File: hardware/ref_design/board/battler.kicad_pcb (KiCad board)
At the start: 2 copper layers, 73.4 x 151.5 mm, 173 parts, among them J1 TYPE-C-31-M-12, J2 53261-0271, J3 FH12-50S-0.5SH(55), J4 SM02B-SRSS-TB, J5 SWD, J7 DEBUG PADS, Q1 2N7002, Q3 2N7002, Q5 AO3400A, Q6 AO3400A, Q7 2N7002, SW1 P1 UP, SW10 P2 DOWN, SW11 P2 LEFT, SW12 P2 RIGHT, SW13 P2 A, SW14 P2 B, SW15 P2 X, SW16 P2 Y, SW18 BOOTSEL, SW19 RESET, SW2 P1 DOWN, SW20 P1 SELECT, SW21 P1 START / PWR, SW22 P2 SELECT, SW23 P2 START / PWR, SW3 P1 LEFT, SW4 P1 RIGHT, SW5 P1 A, SW6 P1 B, SW7 P1 X, SW8 P1 Y, SW9 P2 UP, U1 SRV05-4, U10 MCP6001, U2 BQ24073RGTR, U3 RT9013-33GB, U4 RP2354B, U6 MCP6002, U7 FM8002A, U8 SN74HC165PWR, U9 SN74HC165PWR, X1 12MHz

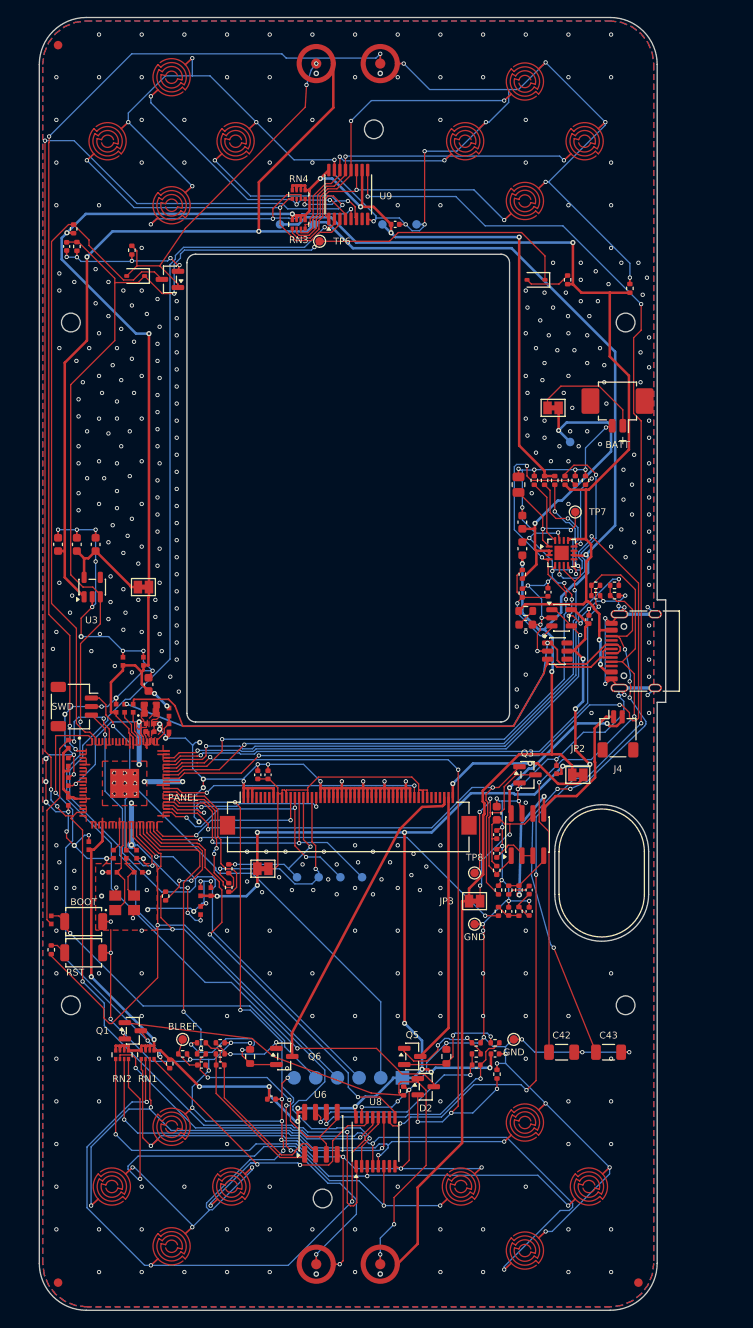
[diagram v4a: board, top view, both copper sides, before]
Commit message: ref_design ESP32-S3: first placement (module, microSD slot with trimmed front tabs, series resistors, third register; case grow_l 1.5 for the shell tabs' copper edge), BOOT/RESET buttons dropped (J7 pads stay), place_new.py, antenna keepout, module GND vias; not routed
Co-Authored-By: Claude Sonnet 5.5 <noreply@anthropic.com>
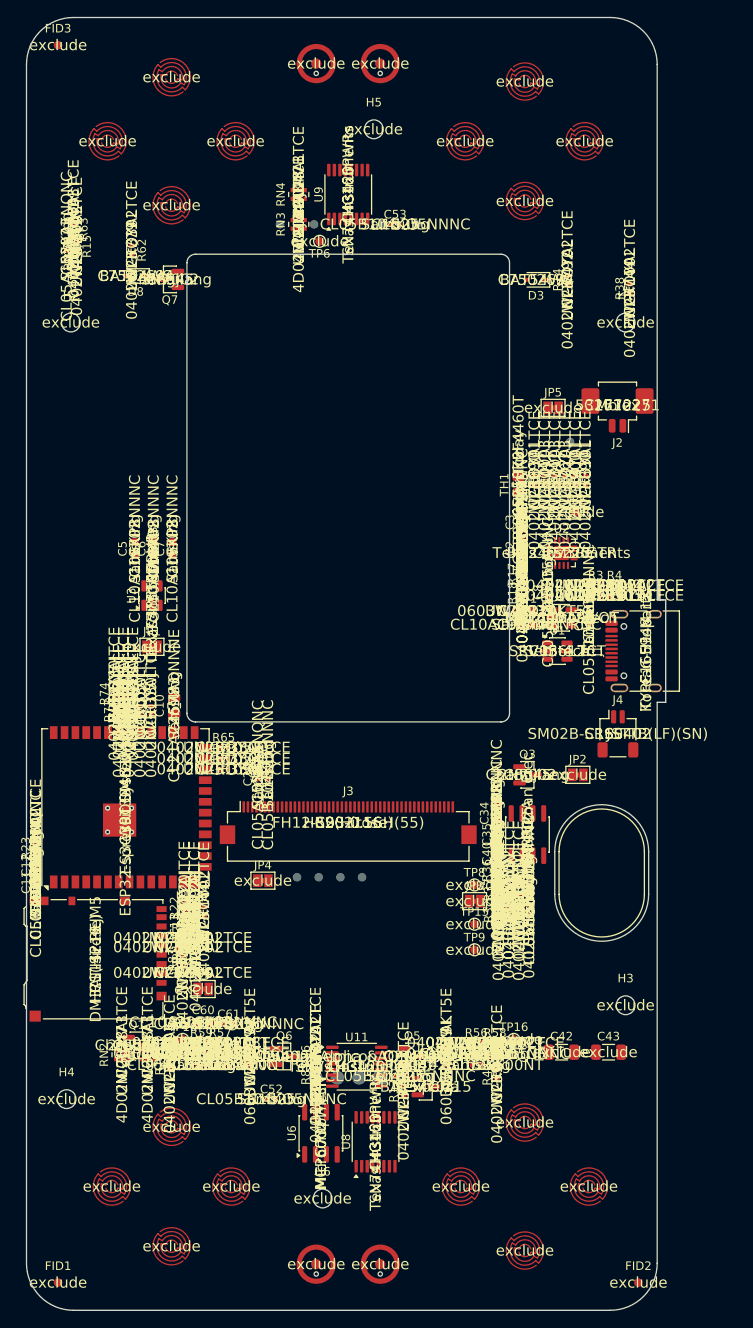
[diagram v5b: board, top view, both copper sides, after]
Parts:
- removed C15, C16, C17, C18, C19, C20, C21, C22: 100n, battler:C_0402_1005Metric_RPi
- removed C23: 10u, Capacitor_SMD:C_0603_1608Metric
- removed C24, C25: 4.7u, battler:C_0402_1005Metric_RPi_Wide
- removed C26: 4.7u, battler:C_0402_1005Metric_RPi
- removed C27, C28: 15p, battler:C_0402_1005Metric_RPi
- removed J5: SWD, battler:JST_SH_SM03B-SRSS-TB_1x03-1MP_P1.00mm_Horizontal
- removed L2: 3.3u, battler:AOTA-B201610S3R3-101-T
- removed R19: 33, battler:R_0402_1005Metric_RPi
- removed R20, R25: 1k, battler:R_0402_1005Metric_RPi
- removed R26: 1k, Resistor_SMD:R_0402_1005Metric
- removed R28, R29: 33, Resistor_SMD:R_0402_1005Metric
- removed SW18: BOOTSEL, battler:SW_SPST_TS-1088-xR020
- removed SW19: RESET, battler:SW_SPST_TS-1088-xR020
- removed X1: 12MHz, battler:ABM8-272-T3
- added C60: 10u, Capacitor_SMD:C_0603_1608Metric, F.Cu at (83.0, 142.0)
- added C61: 100n, Capacitor_SMD:C_0402_1005Metric, F.Cu at (86.0, 142.2)
- added C62: 100n, Capacitor_SMD:C_0402_1005Metric, F.Cu at (106.1, 148.3)
- added J8: DM3AT-SF-PEJM5, battler:microSD_HC_Hirose_DM3AT-SF-PEJM5, F.Cu at (70.4, 134.6)
- added JP6: Bridged, Jumper:SolderJumper-2_P1.3mm_Bridged_Pad1.0x1.5mm, F.Cu at (83.0, 138.1)
- added R70: 33, Resistor_SMD:R_0402_1005Metric, F.Cu at (76.9, 105.5)
- added R71: 33, Resistor_SMD:R_0402_1005Metric, F.Cu at (75.6, 105.5)
- added R72: 33, Resistor_SMD:R_0402_1005Metric, F.Cu at (74.3, 105.5)
- added R73: 33, Resistor_SMD:R_0402_1005Metric, F.Cu at (73.1, 105.5)
- added R74: 33, Resistor_SMD:R_0402_1005Metric, F.Cu at (72.6, 103.5)
- added R75: 33, Resistor_SMD:R_0402_1005Metric, F.Cu at (73.7, 103.5)
- added R76: 33, Resistor_SMD:R_0402_1005Metric, F.Cu at (74.8, 103.5)
- added R77: 33, Resistor_SMD:R_0402_1005Metric, F.Cu at (85.4, 112.4)
- added R78: 33, Resistor_SMD:R_0402_1005Metric, F.Cu at (85.4, 111.1)
- added R79: 10k, Resistor_SMD:R_0402_1005Metric, F.Cu at (83.1, 129.0)
- added R80: 10k, Resistor_SMD:R_0402_1005Metric, F.Cu at (80.6, 132.1)
- added R81: 10k, Resistor_SMD:R_0402_1005Metric, F.Cu at (82.1, 132.6)
- added R82: 10k, Resistor_SMD:R_0402_1005Metric, F.Cu at (80.6, 133.2)
- added R83: 10k, Resistor_SMD:R_0402_1005Metric, F.Cu at (80.6, 134.7)
- added R84: 10k, Resistor_SMD:R_0402_1005Metric, F.Cu at (80.6, 136.2)
- added R86: 47k, Resistor_SMD:R_0402_1005Metric, F.Cu at (96.2, 146.0)
- added R87: 47k, Resistor_SMD:R_0402_1005Metric, F.Cu at (96.2, 148.0)
- added U11: SN74HC165PWR, Package_SO:TSSOP-16_4.4x5mm_P0.65mm, F.Cu at (101.0, 147.2)
- C10: value 100n -> 22u; footprint battler:C_0402_1005Metric_RPi -> Capacitor_SMD:C_0805_2012Metric
- C11: footprint battler:C_0402_1005Metric_RPi -> Capacitor_SMD:C_0402_1005Metric
- C12: value 100n -> 1u; footprint battler:C_0402_1005Metric_RPi -> Capacitor_SMD:C_0402_1005Metric
- C13, C14: value 100n -> DNP; footprint battler:C_0402_1005Metric_RPi -> Capacitor_SMD:C_0402_1005Metric
- J7: footprint battler:Pogo_Pads_1x06_P2.54mm -> battler:Pogo_Pads_1x04_P2.54mm
- R21, R22: value 27 -> 22; footprint battler:R_0402_1005Metric_RPi -> Resistor_SMD:R_0402_1005Metric
- R23: footprint battler:R_0402_1005Metric_RPi -> Resistor_SMD:R_0402_1005Metric
- R32, R33: value 1k -> 1.5k
- TP11: value LCD_SCK -> LCD_WR
- TP12: value LCD_MOSI -> LCD_DC
- TP13: value LCD_CS -> LCD_D0
- TP14: value LCD_DC -> LCD_TE
- TP9: value +1V1 -> AUDIO_PWM; moved to F.Cu
- U3: value RT9013-33GB -> TLV75733PDBVR
- U4: value RP2354B -> ESP32-S3-WROOM-1U-N16R8; footprint battler:RP2350B_QFN80_RPi -> battler:ESP32-S3-WROOM-1U
- moved C10 45.4 mm to (79.6, 104.9)
- moved TP9 42.0 mm to (114.8, 133.5), turned to 0 degrees
- moved C13 31.3 mm to (80.8, 130.6)
- moved R21 24.8 mm to (82.0, 128.6), turned to 90 degrees
- moved C14 24.2 mm to (82.0, 130.6)
- moved R22 24.2 mm to (80.8, 128.6), turned to 90 degrees
- moved C11 22.5 mm to (63.4, 125.6)
- moved R65 18.7 mm to (85.4, 109.8), turned to 0 degrees
- moved R23 12.8 mm to (63.4, 121.6)
- moved H4 11.0 mm to (67.0, 151.0)
- moved C12 9.19 mm to (63.4, 123.6), turned to 90 degrees
- moved C5 9.01 mm to (75.0, 86.5)
- moved C6 9.01 mm to (77.2, 86.5)
- moved C7 9.01 mm to (79.4, 86.5)
- moved JP1 7.07 mm to (77.0, 98.0)
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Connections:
- net /Display/LCD_SCK renamed /Display/LCD_WR
- C12 pad 1: +3V3 -> EN
- C13 pad 1: +3V3 -> /MCU/USB_DP_MCU
- C14 pad 1: +3V3 -> /MCU/USB_DM_MCU
- J3 pad 13: LCD_CS -> GND
- J3 pad 17: /Display/LCD_MOSI -> GND
- J3 pad 18: LCD_MISO -> unconnected-(J3-Pin_18-Pad18)
- J3 pad 19: GND -> /Display/LCD_D0
- J3 pad 20: GND -> /Display/LCD_D1
- J3 pad 21: GND -> /Display/LCD_D2
- J3 pad 22: GND -> /Display/LCD_D3
- J3 pad 23: GND -> /Display/LCD_D4
- J3 pad 24: GND -> /Display/LCD_D5
- J3 pad 25: GND -> /Display/LCD_D6
- J3 pad 26: GND -> /Display/LCD_D7
- J3 pad 42: /Display/LCD_3V3 -> GND
- J7 pad 2: SWCLK -> EN
- J7 pad 3: SWDIO -> BOOT
- J7 pad 4: RUN -> GND
- R23 pad 2: QSPI_SS -> EN
- SW20 pad 1: P1_SELECT -> /Buttons/P1_SELECT
- SW22 pad 1: P2_SELECT -> /Buttons/P2_SELECT
- TP12 pad 1: /Display/LCD_MOSI -> LCD_DC
- TP13 pad 1: LCD_CS -> /Display/LCD_D0
- TP14 pad 1: LCD_DC -> LCD_TE
- TP9 pad 1: +1V1 -> AUDIO_PWM
- U4 pad 1: P2_SELECT -> GND
- U4 pad 10: +1V1 -> SD_CD
- U4 pad 11: unconnected-(U4-GPIO12-Pad11) -> SR_CLK_MCU
- U4 pad 12: unconnected-(U4-GPIO13-Pad12) -> AUDIO_PWM
- U4 pad 13: unconnected-(U4-GPIO14-Pad13) -> /MCU/USB_DM_MCU
- U4 pad 14: unconnected-(U4-GPIO15-Pad14) -> /MCU/USB_DP_MCU
- U4 pad 15: +3V3 -> SR_DATA
- U4 pad 16: unconnected-(U4-GPIO16-Pad16) -> CHG_OFF
- U4 pad 17: unconnected-(U4-GPIO17-Pad17) -> BL_PWM
- U4 pad 18: unconnected-(U4-GPIO18-Pad18) -> LCD_TE
- U4 pad 19: SR_PL -> SD_CMD
- U4 pad 2: unconnected-(U4-GPIO5-Pad2) -> +3V3
- U4 pad 20: unconnected-(U4-GPIO20-Pad20) -> SD_CLK
- U4 pad 21: unconnected-(U4-GPIO21-Pad21) -> SD_D0
- U4 pad 22: unconnected-(U4-GPIO22-Pad22) -> SD_D1
- U4 pad 23: unconnected-(U4-GPIO23-Pad23) -> PWR_HOLD
- U4 pad 24: +3V3 -> LCD_D7_MCU
- U4 pad 25: unconnected-(U4-GPIO24-Pad25) -> LCD_WR_MCU
- U4 pad 26: unconnected-(U4-GPIO25-Pad26) -> AMP_EN
- U4 pad 27: unconnected-(U4-GPIO26-Pad27) -> BOOT
- U4 pad 29: +3V3 -> unconnected-(U4-IO36-Pad29)
- U4 pad 3: unconnected-(U4-GPIO6-Pad3) -> EN
- U4 pad 30: /MCU/XIN -> unconnected-(U4-IO37-Pad30)
- U4 pad 31: /MCU/XOUT -> LCD_D0_MCU
- U4 pad 32: +1V1 -> LCD_D1_MCU
- U4 pad 33: SWCLK -> LCD_D2_MCU
- U4 pad 34: SWDIO -> LCD_D3_MCU
- U4 pad 35: RUN -> LCD_D4_MCU
- U4 pad 36: BL_PWM -> LCD_D6_MCU
- U4 pad 37: SR_CLK_MCU -> LCD_D5_MCU
- U4 pad 38: SR_DATA -> CC1_SENSE
- U4 pad 39: AUDIO_PWM -> VBAT_SENSE
- U4 pad 4: unconnected-(U4-GPIO7-Pad4) -> CC2_SENSE
- U4 pad 40: LCD_TE -> GND
- U4 pad 41: +3V3 -> GND
- U4 pad 5: +3V3 -> SR_PL
- U4 pad 6: unconnected-(U4-GPIO8-Pad6) -> LCD_DC
- U4 pad 7: unconnected-(U4-GPIO9-Pad7) -> LCD_RST
- U4 pad 8: unconnected-(U4-GPIO10-Pad8) -> SD_D2
- U4 pad 9: unconnected-(U4-GPIO11-Pad9) -> SD_D3
- U9 pad 10: +3V3 -> /Buttons/SR_CHAIN2
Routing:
- net GND: track 750.2 -> 0.00 mm, vias 498 -> 4
- net +3V3: track 406.7 -> 0.00 mm, vias 28 -> 0
- net VSYS: track 273.5 -> 0.00 mm, vias 5 -> 0
- net SR_PL: track 199.7 -> 0.00 mm, vias 6 -> 0
- net /Power/PWR_EN: track 195.4 -> 0.00 mm, vias 4 -> 0
- net /Buttons/SR_CLK: track 162.0 -> 0.00 mm, vias 3 -> 0
- net /Buttons/SR_CHAIN: track 158.7 -> 0.00 mm, vias 6 -> 0
- net P2_SELECT: track 118.5 -> 0.00 mm, vias 4 -> 0
- net VBUS: track 113.0 -> 0.00 mm, vias 3 -> 0
- net CHG_STAT_N: track 102.8 -> 0.00 mm, vias 5 -> 0
- net PWR_HOLD: track 91.1 -> 0.00 mm, vias 5 -> 0
- net CHG_OFF: track 88.8 -> 0.00 mm, vias 4 -> 0
- net CHG_PG_N: track 80.4 -> 0.00 mm, vias 4 -> 0
- net P2_START: track 78.7 -> 0.00 mm
- net SWCLK: track 78.6 -> 0.00 mm, vias 2 -> 0
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- removed copper zone on F.Cu, net +1V1
- removed copper zone on F.Cu, net +3V3
- removed copper zone on B.Cu, net GND
- removed copper zone on F.Cu, net GND
- removed copper zone on F.Cu, net VREG_LX
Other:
- board size 73.4 x 151.5 mm -> 74.9 x 151.5 mm
- board text removed: "+"
- board text removed: "1V1"
- board text removed: "2 LAYERS 1.6 MM ENIG"
- board text removed: "3V3"
- board text removed: "BATT"
- board text removed: "BLREF"
- board text removed: "BOOT"
- board text removed: "CS"
- board text removed: "DC"
- board text removed: "GND"
- board text removed: "MOSI"
- board text removed: "PANEL"
- board text removed: "REV 1"
- board text removed: "RST"
- board text removed: "SCK"
- board text removed: "SWD"
- board text removed: "SWD PADS"
- board text removed: "TWO-PLAYER HANDHELD REF-A"
- board text removed: "VBAT"
- board text removed: "VBUS"
- board text removed: "VSYS"

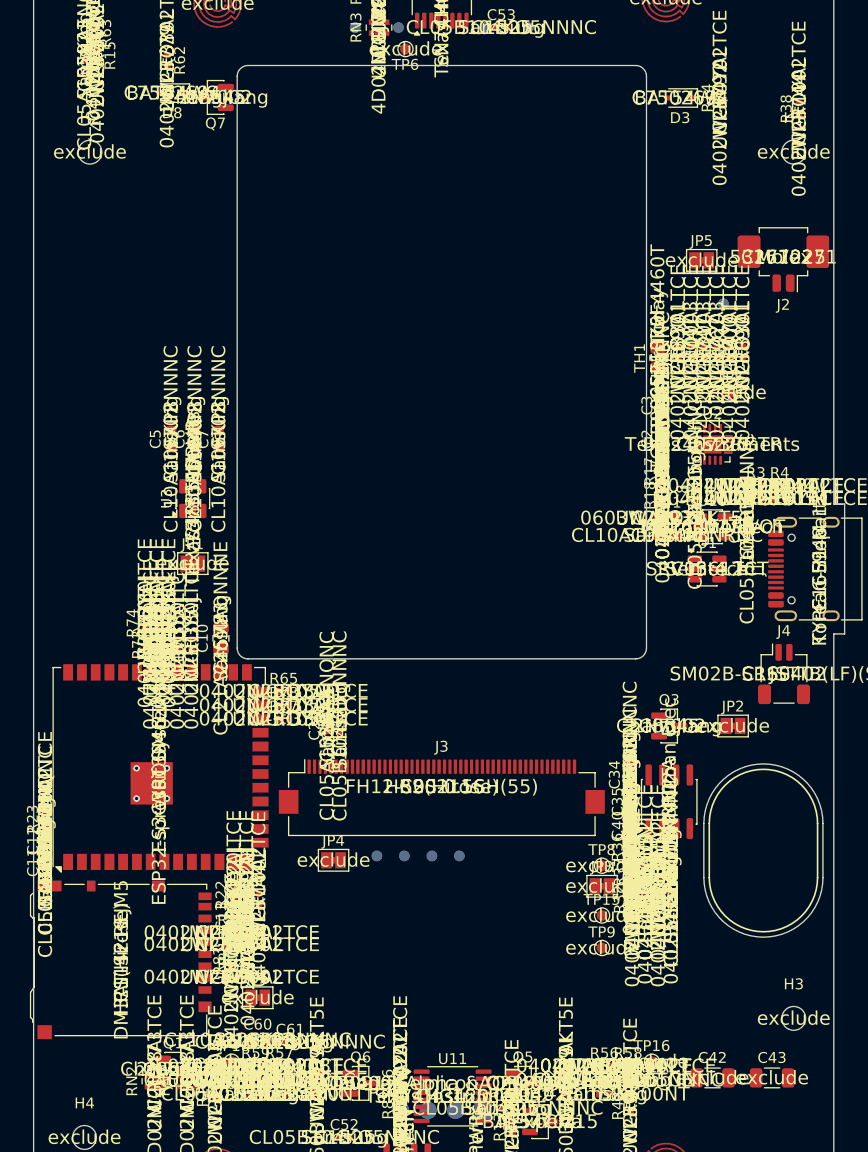
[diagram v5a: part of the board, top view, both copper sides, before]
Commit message: ref_design ESP32-S3 placement: module, microSD slot, nearest-legal-spot search for the new parts (tools/place_new.py), cell hole 38.2 x 55.2 (V&V C1), U2 on TI's RGT0016C land (P3), net classes for CELL_P, AMP_VDD, VBUS_C1 (P4), comb keep-out 2.9 flats (B3), check_fit module body; check_fit PASS, placement DRC clean
Co-Authored-By: Claude Sonnet 5.5 <noreply@anthropic.com>
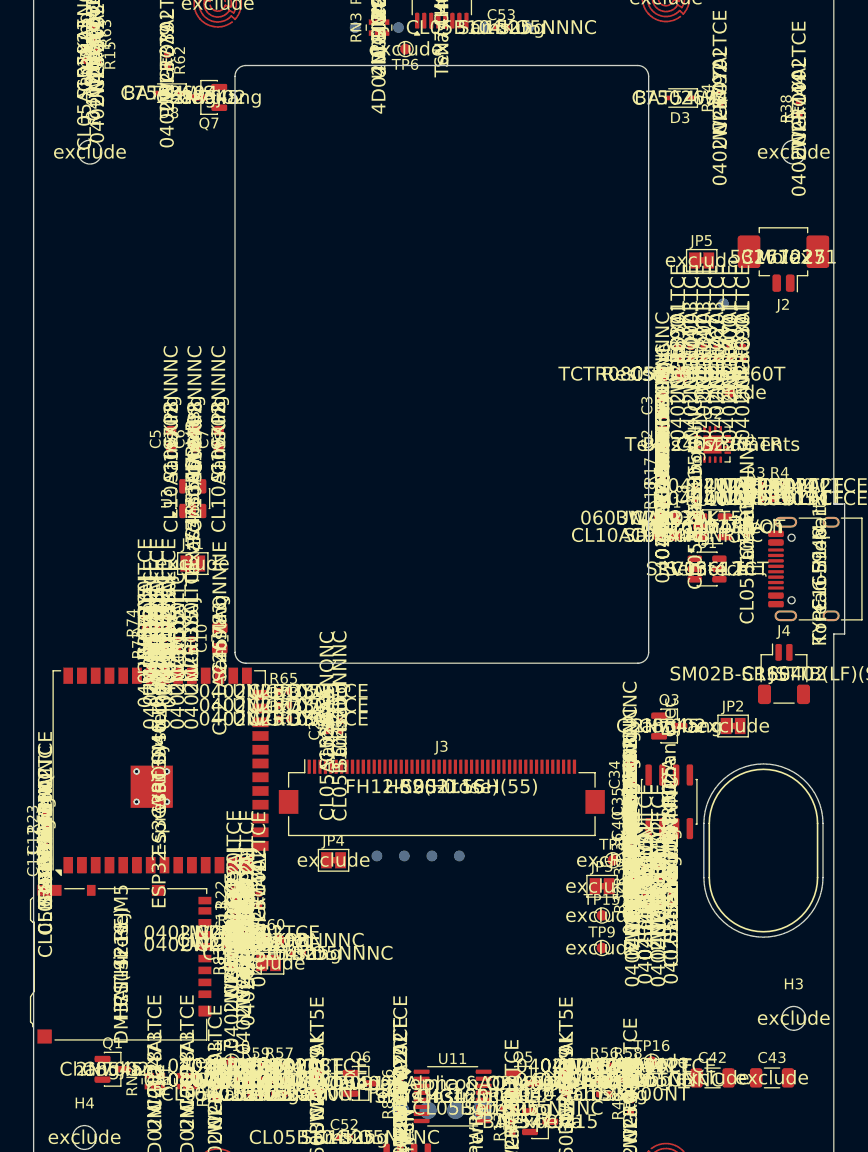
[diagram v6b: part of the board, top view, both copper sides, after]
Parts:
- U2: footprint Package_DFN_QFN:VQFN-16-1EP_3x3mm_P0.5mm_EP1.68x1.68mm -> battler:VQFN-16-1EP_3x3mm_RGT0016C
- moved C60 9.28 mm to (84.2, 132.8)
- moved C61 8.23 mm to (86.7, 134.0)
- moved Q1 5.60 mm to (69.6, 144.7)
- moved JP6 3.35 mm to (84.0, 134.9)
- moved TH1 1.98 mm to (121.2, 80.5), turned to 0 degrees
- moved R84 1.49 mm to (81.7, 135.2), turned to 90 degrees
- moved TP8 1.12 mm to (115.8, 125.4)
- moved Q7 0.60 mm to (78.5, 54.9)
- moved J8 0.40 mm to (70.4, 135.0)
- moved D8 0.30 mm to (74.8, 54.5)
- moved U4 0.30 mm to (73.9, 117.1)
- moved C10 0.10 mm to (79.5, 104.9)
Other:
- outline, holes or cut-outs redrawn

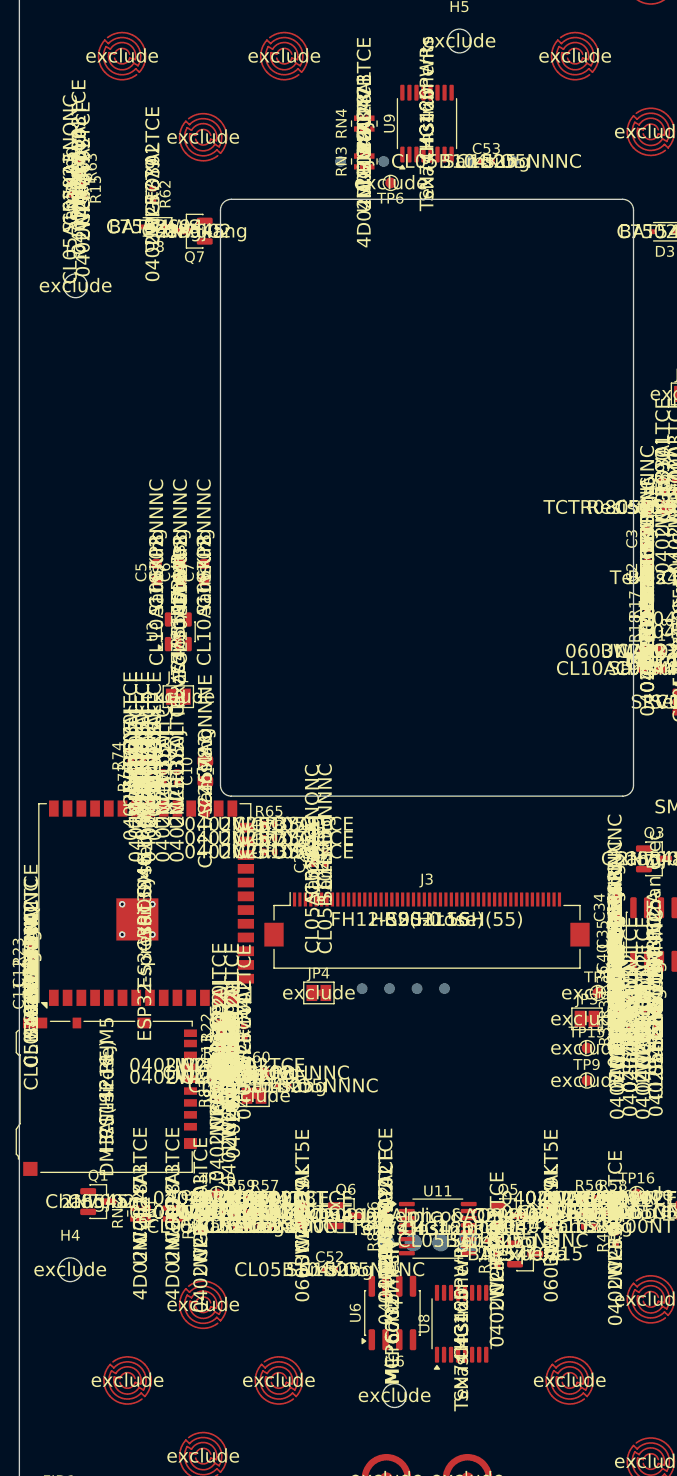
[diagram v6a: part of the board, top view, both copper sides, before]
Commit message: ref_design ESP32-S3: power key in seat 1's deck (case.scad pwr_* parameters, pocket, hole, flange recess, printed cap, check_power_key.py, asserts), SW24 and R88 placed, R63 moved to U11, Q7/D8/R62 gone from the placement; case checks pass (manifold 49, wall, buttons 11 known), check_fit PASS, placement DRC clean
Co-Authored-By: Claude Sonnet 5.5 <noreply@anthropic.com>
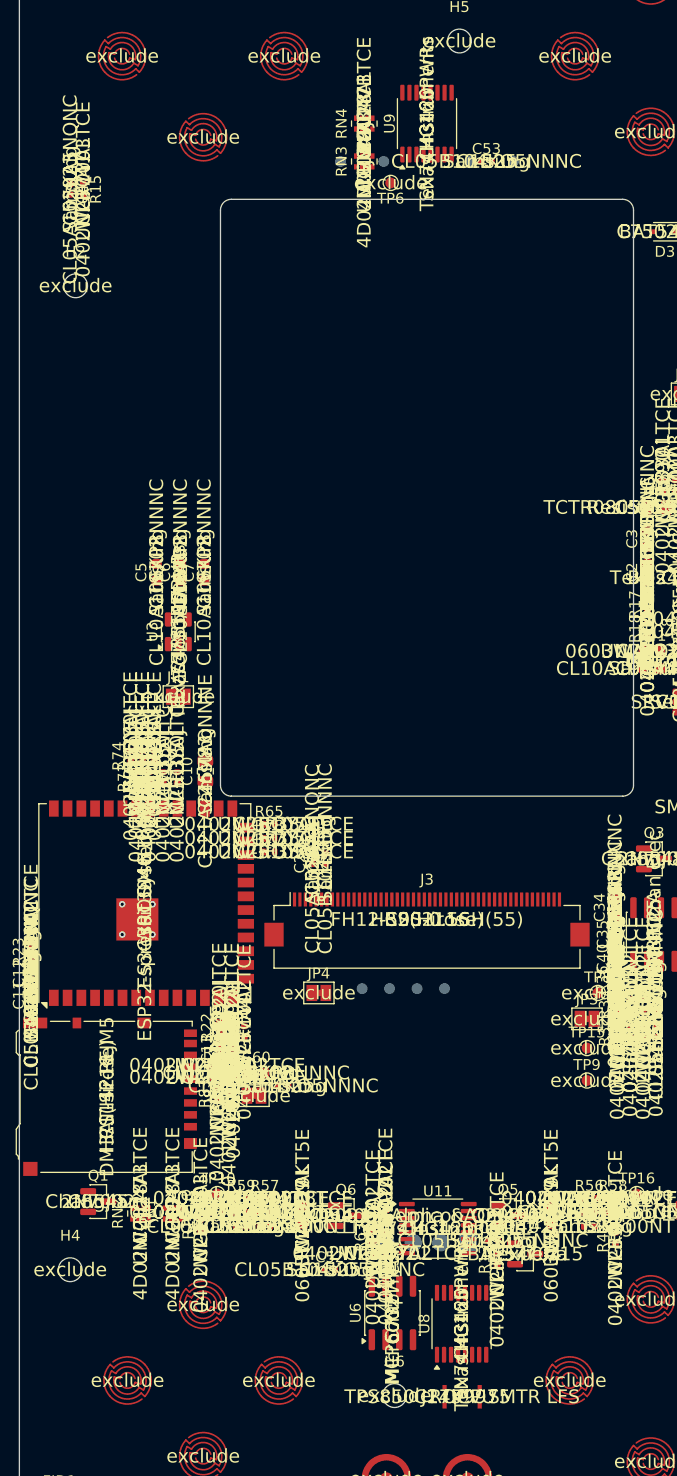
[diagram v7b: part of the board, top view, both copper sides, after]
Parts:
- removed D8: BAT54WS, Diode_SMD:D_SOD-323
- removed Q7: 2N7002, Package_TO_SOT_SMD:SOT-23
- removed R62: 33k, Resistor_SMD:R_0402_1005Metric
- added R88: 47k, Resistor_SMD:R_0402_1005Metric, F.Cu at (95.7, 149.5)
- added SW24: POWER, battler:Tact_ROCPU_TPS850, F.Cu at (103.2, 162.8)
- R63: value 100k -> 47k
- SW21: value P1 START / PWR -> P1 START
- SW23: value P2 START / PWR -> P2 START
- moved R63 102.6 mm to (95.0, 148.0), turned to 90 degrees
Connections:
- R63 pad 1: P2_START -> +3V3
- R63 pad 2: +3V3 -> /Buttons/P2_START
- SW21 pad 1: PWR_BTN_RAW -> /Buttons/P1_START
- SW21 pad 2: VSYS -> GND
- SW23 pad 1: P2_START_RAW -> /Buttons/P2_START
- SW23 pad 2: VSYS -> GND
- U11 pad 12: +3V3 -> /Buttons/P1_START
- U11 pad 5: P2_START -> /Buttons/P2_START
